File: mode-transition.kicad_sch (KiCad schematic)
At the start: 17 parts, among them Q19001 DNLS350E, U19001 4081, U19002 4073, U19003 4075, U19004 4081, U19005 4073, U19006 4075, U19007 4069

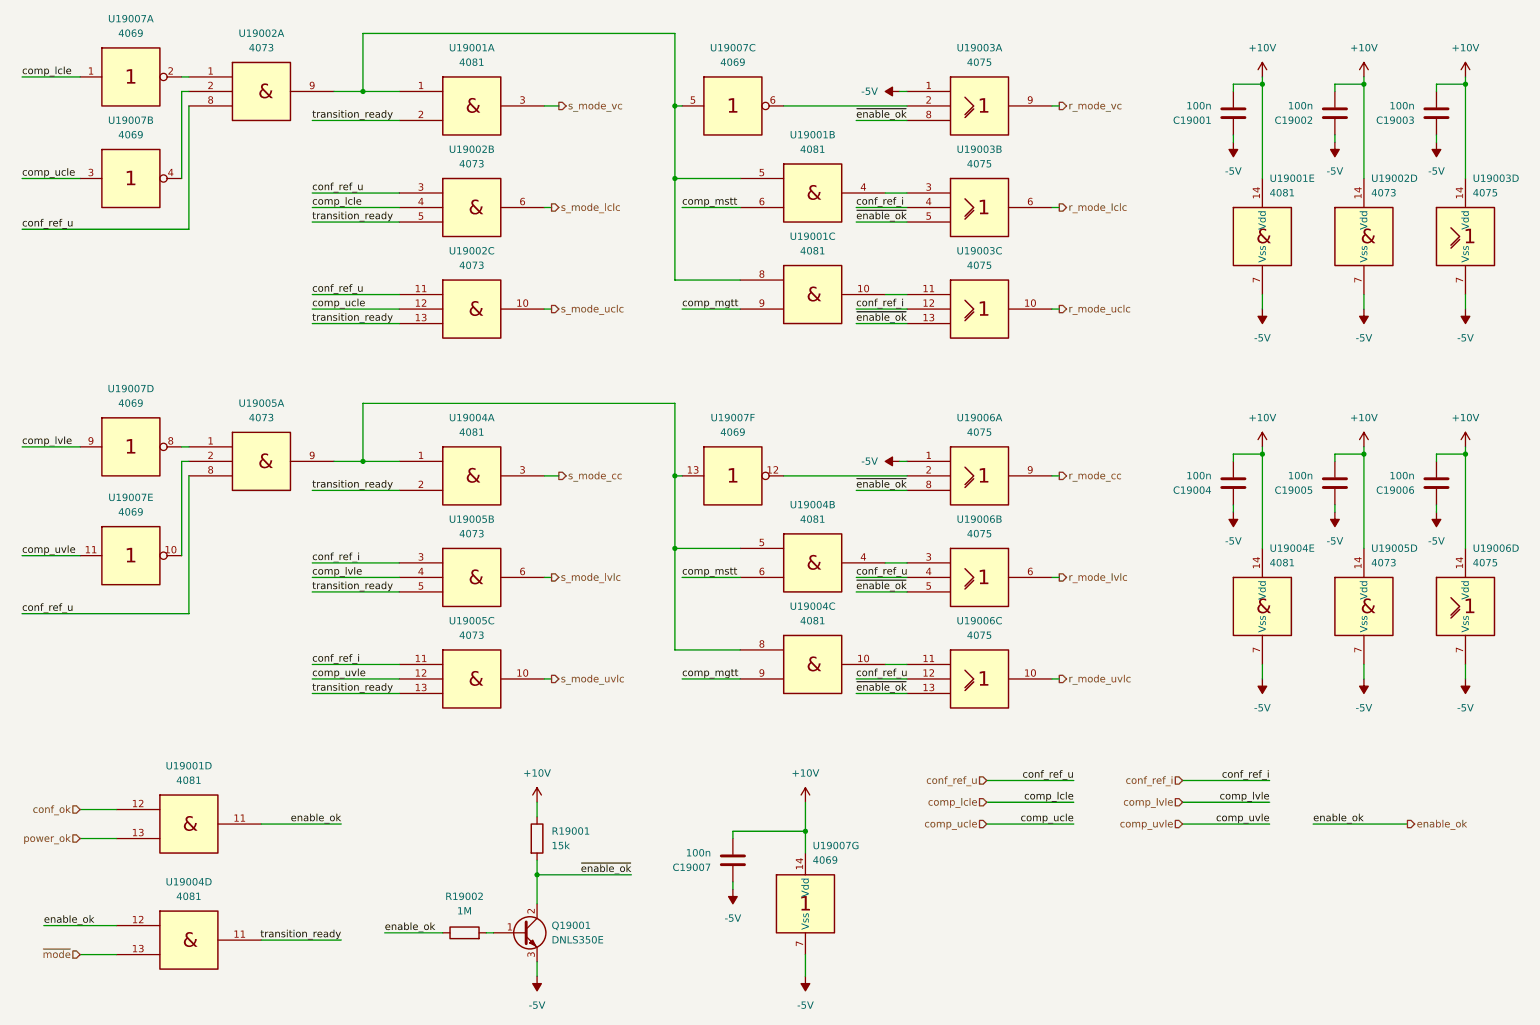
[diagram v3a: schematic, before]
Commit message: add limit-logic compare-logic hierachical sheet and hirarchy connectors
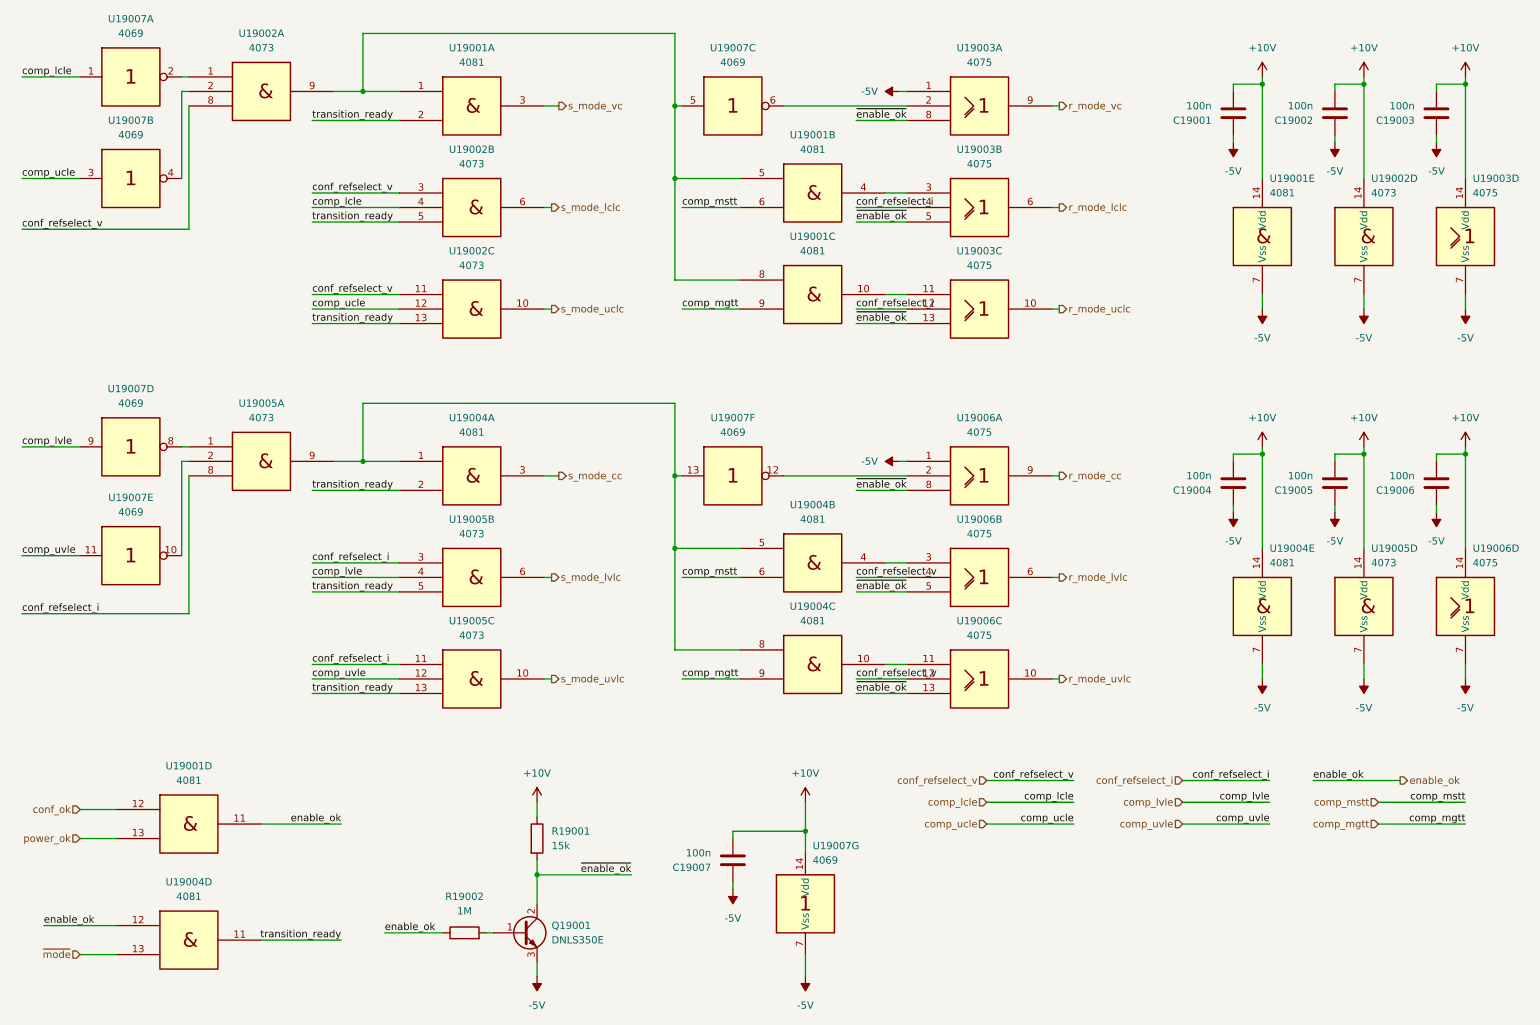
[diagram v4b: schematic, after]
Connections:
- net conf_ref_i renamed conf_refselect_i
- net conf_refselect_i: now also U19005.8
- net conf_ref_u renamed conf_refselect_v
- net conf_refselect_v: no longer U19005.8
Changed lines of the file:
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@@
+	(wire
+		(pts
+			(xy 257.81 160.02) (xy 273.05 160.02)
+		)
+		(stroke
+			(width 0)
+			(type default)
+		)
+	)
 	(wire
 		(pts
@@
 	(wire
 		(pts
+			(xy 49.53 99.06) (xy 49.53 123.19)
+		)
+		(stroke
+			(width 0)
+			(type default)
+		)
+	)
+	(wire
+		(pts
 			(xy 250.19 39.37) (xy 250.19 40.64)
 		)
@@
 	(wire
 		(pts
-			(xy 246.38 160.02) (xy 262.89 160.02)
+			(xy 246.38 152.4) (xy 261.62 152.4)
+		)
+		(stroke
+			(width 0)
+			(type default)
+		)
+	)
+	(wire
+		(pts
+			(xy 257.81 156.21) (xy 273.05 156.21)
 		)
 		(stroke
@@
 	(wire
 		(pts
-			(xy 49.53 123.19) (xy 49.53 99.06)
-		)
-		(stroke
-			(width 0)
-			(type default)
-		)
-	)
-	(wire
-		(pts
 			(xy 49.53 55.88) (xy 49.53 34.29)
 		)
@@
 			(width 0)
 			(type default)
+		)
+	)
+	(label "comp_mstt"
+		(at 273.05 156.21 180)
+		(fields_autoplaced yes)
+		(effects
+			(font
+				(size 1.27 1.27)
+			)
+			(justify right bottom)
 		)
 	)
@@
 		)
 	)
-	(label "conf_ref_i"
+	(label "conf_refselect_i"
 		(at 71.12 114.3 0)
 		(fields_autoplaced yes)
@@
 		)
 	)
-	(label "conf_ref_i"
+	(label "conf_refselect_i"
 		(at 166.37 52.07 0)
 		(fields_autoplaced yes)
@@
 		)
 	)
-	(label "conf_ref_u"
+	(label "conf_refselect_i"
 		(at 20.32 123.19 0)
 		(fields_autoplaced yes)
@@
 		)
 	)
-	(label "conf_ref_u"
+	(label "conf_refselect_v"
 		(at 204.47 152.4 180)
 		(fields_autoplaced yes)
@@
 		)
 	)
-	(label "conf_ref_i"
+	(label "conf_refselect_i"
 		(at 238.76 152.4 180)
 		(fields_autoplaced yes)
@@
 		)
 	)
-	(label "conf_ref_u"
+	(label "comp_mgtt"
+		(at 273.05 160.02 180)
+		(fields_autoplaced yes)
+		(effects
+			(font
+				(size 1.27 1.27)
+			)
+			(justify right bottom)
+		)
+	)
+	(label "conf_refselect_v"
 		(at 71.12 67.31 0)
 		(fields_autoplaced yes)
@@
 		)
 	)
-	(label "conf_ref_u"
+	(label "conf_refselect_v"
 		(at 166.37 134.62 0)
 		(fields_autoplaced yes)
@@
 		)
 	)
-	(label "conf_ref_i"
+	(label "conf_refselect_i"
 		(at 166.37 69.85 0)
 		(fields_autoplaced yes)
@@
 	)
 	(label "enable_ok"
-		(at 246.38 160.02 0)
+		(at 246.38 152.4 0)
 		(fields_autoplaced yes)
 		(effects
@@
 		)
 	)
-	(label "conf_ref_u"
+	(label "conf_refselect_v"
 		(at 71.12 49.53 0)
 		(fields_autoplaced yes)
@@
 		)
 	)
-	(label "conf_ref_i"
+	(label "conf_refselect_i"
 		(at 71.12 132.08 0)
 		(fields_autoplaced yes)
@@
 		)
 	)
-	(label "conf_ref_u"
+	(label "conf_refselect_v"
 		(at 166.37 116.84 0)
 		(fields_autoplaced yes)
@@
 		)
 	)
-	(label "conf_ref_u"
+	(label "conf_refselect_v"
 		(at 20.32 55.88 0)
 		(fields_autoplaced yes)
@@
 	(hierarchical_label "enable_ok"
 		(shape output)
-		(at 262.89 160.02 0)
+		(at 261.62 152.4 0)
 		(fields_autoplaced yes)
 		(effects
@@
 		)
 	)
+	(hierarchical_label "comp_mgtt"
+		(shape input)
+		(at 257.81 160.02 180)
+		(fields_autoplaced yes)
+		(effects
+			(font
+				(size 1.27 1.27)
+			)
+			(justify right)
+		)
+	)
 	(hierarchical_label "s_mode_uvlc"
 		(shape output)
@@
 		)
 	)
+	(hierarchical_label "comp_mstt"
+		(shape input)
+		(at 257.81 156.21 180)
+		(fields_autoplaced yes)
+		(effects
+			(font
+				(size 1.27 1.27)
+			)
+			(justify right)
+		)
+	)
 	(hierarchical_label "r_mode_lvlc"
 		(shape output)
@@
 		)
 	)
-	(hierarchical_label "conf_ref_u"
+	(hierarchical_label "conf_refselect_v"
 		(shape input)
 		(at 189.23 152.4 180)
@@
 		)
 	)
-	(hierarchical_label "conf_ref_i"
+	(hierarchical_label "conf_refselect_i"
 		(shape input)
 		(at 223.52 152.4 180)

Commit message: fix missing footprints, MPN, VPN and datasheet info in BOM
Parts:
- Q19001: footprint (none) -> Package_TO_SOT_SMD:SOT-223-3_TabPin2; MPN (none) -> DNLS350E-13; VPN (none) -> 621-DNLS350E-13
- U19003, U19006: footprint (none) -> Package_SO:SOIC-14_3.9x8.7mm_P1.27mm; MPN (none) -> CD4075BM96; VPN (none) -> 595-CD4075BM96
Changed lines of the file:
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@@
 			)
 		)
-		(property "Footprint" ""
+		(property "Footprint" "Package_SO:SOIC-14_3.9x8.7mm_P1.27mm"
 			(at 273.05 121.92 0)
 			(effects
@@
 			)
 		)
-		(property "Datasheet" ""
+		(property "Datasheet" "https://www.ti.com/lit/ds/symlink/cd4075b.pdf"
 			(at 273.05 121.92 0)
 			(effects
@@
 			)
 		)
+		(property "MPN" "CD4075BM96"
+			(at 273.05 121.92 0)
+			(effects
+				(font
+					(size 1.27 1.27)
+				)
+				(hide yes)
+			)
+		)
+		(property "VPN" "595-CD4075BM96"
+			(at 273.05 121.92 0)
+			(effects
+				(font
+					(size 1.27 1.27)
+				)
+				(hide yes)
+			)
+		)
 		(pin "1"
 		)
@@
 			)
 		)
-		(property "Footprint" ""
+		(property "Footprint" "Package_SO:SOIC-14_3.9x8.7mm_P1.27mm"
 			(at 187.96 99.06 0)
 			(effects
@@
 			)
 		)
-		(property "Datasheet" ""
+		(property "Datasheet" "https://www.ti.com/lit/ds/symlink/cd4075b.pdf"
 			(at 187.96 99.06 0)
 			(effects
@@
 			)
 		)
+		(property "MPN" "CD4075BM96"
+			(at 187.96 99.06 0)
+			(effects
+				(font
+					(size 1.27 1.27)
+				)
+				(hide yes)
+			)
+		)
+		(property "VPN" "595-CD4075BM96"
+			(at 187.96 99.06 0)
+			(effects
+				(font
+					(size 1.27 1.27)
+				)
+				(hide yes)
+			)
+		)
 		(pin "1"
 		)
@@
 			)
 		)
-		(property "Footprint" ""
+		(property "Footprint" "Package_SO:SOIC-14_3.9x8.7mm_P1.27mm"
 			(at 273.05 57.15 0)
 			(effects
@@
 			)
 		)
-		(property "Datasheet" ""
+		(property "Datasheet" "https://www.ti.com/lit/ds/symlink/cd4075b.pdf"
 			(at 273.05 57.15 0)
 			(effects
@@
 			)
 		)
+		(property "MPN" "CD4075BM96"
+			(at 273.05 57.15 0)
+			(effects
+				(font
+					(size 1.27 1.27)
+				)
+				(hide yes)
+			)
+		)
+		(property "VPN" "595-CD4075BM96"
+			(at 273.05 57.15 0)
+			(effects
+				(font
+					(size 1.27 1.27)
+				)
+				(hide yes)
+			)
+		)
 		(pin "1"
 		)
@@
 			)
 		)
-		(property "Footprint" ""
+		(property "Footprint" "Package_TO_SOT_SMD:SOT-223-3_TabPin2"
 			(at 113.03 176.53 0)
 			(effects
@@
 			)
 		)
-		(property "Datasheet" "~"
+		(property "Datasheet" "https://www.diodes.com/assets/Datasheets/ds31231.pdf"
 			(at 107.95 179.07 0)
 			(effects
@@
 			)
 		)
-		(property "MPN" ""
+		(property "MPN" "DNLS350E-13"
 			(at 107.95 179.07 0)
 			(effects
@@
 			)
 		)
-		(property "VPN" ""
+		(property "VPN" "621-DNLS350E-13"
 			(at 107.95 179.07 0)
 			(effects
@@
 			)
 		)
-		(property "Footprint" ""
+		(property "Footprint" "Package_SO:SOIC-14_3.9x8.7mm_P1.27mm"
 			(at 187.96 34.29 0)
 			(effects
@@
 			)
 		)
-		(property "Datasheet" ""
+		(property "Datasheet" "https://www.ti.com/lit/ds/symlink/cd4075b.pdf"
 			(at 187.96 34.29 0)
 			(effects
@@
 			)
 		)
+		(property "MPN" "CD4075BM96"
+			(at 187.96 34.29 0)
+			(effects
+				(font
+					(size 1.27 1.27)
+				)
+				(hide yes)
+			)
+		)
+		(property "VPN" "595-CD4075BM96"
+			(at 187.96 34.29 0)
+			(effects
+				(font
+					(size 1.27 1.27)
+				)
+				(hide yes)
+			)
+		)
 		(pin "1"
 		)
@@
 			)
 		)
-		(property "Footprint" ""
+		(property "Footprint" "Package_SO:SOIC-14_3.9x8.7mm_P1.27mm"
 			(at 187.96 116.84 0)
 			(effects
@@
 			)
 		)
-		(property "Datasheet" ""
+		(property "Datasheet" "https://www.ti.com/lit/ds/symlink/cd4075b.pdf"
 			(at 187.96 116.84 0)
 			(effects
@@
 			)
 		)
+		(property "MPN" "CD4075BM96"
+			(at 187.96 116.84 0)
+			(effects
+				(font
+					(size 1.27 1.27)
+				)
+				(hide yes)
+			)
+		)
+		(property "VPN" "595-CD4075BM96"
+			(at 187.96 116.84 0)
+			(effects
+				(font
+					(size 1.27 1.27)
+				)
+				(hide yes)
+			)
+		)
 		(pin "1"
 		)
@@
 			)
 		)
-		(property "Footprint" ""
+		(property "Footprint" "Package_SO:SOIC-14_3.9x8.7mm_P1.27mm"
 			(at 187.96 69.85 0)
 			(effects
@@
 			)
 		)
-		(property "Datasheet" ""
+		(property "Datasheet" "https://www.ti.com/lit/ds/symlink/cd4075b.pdf"
 			(at 187.96 69.85 0)
 			(effects
@@
 			)
 		)
+		(property "MPN" "CD4075BM96"
+			(at 187.96 69.85 0)
+			(effects
+				(font
+					(size 1.27 1.27)
+				)
+				(hide yes)
+			)
+		)
+		(property "VPN" "595-CD4075BM96"
+			(at 187.96 69.85 0)
+			(effects
+				(font
+					(size 1.27 1.27)
+				)
+				(hide yes)
+			)
+		)
 		(pin "1"
 		)
@@
 			)
 		)
-		(property "Footprint" ""
+		(property "Footprint" "Package_SO:SOIC-14_3.9x8.7mm_P1.27mm"
 			(at 187.96 52.07 0)
 			(effects
@@
 			)
 		)
-		(property "Datasheet" ""
+		(property "Datasheet" "https://www.ti.com/lit/ds/symlink/cd4075b.pdf"
 			(at 187.96 52.07 0)
 			(effects
@@
 			)
 		)
+		(property "MPN" "CD4075BM96"
+			(at 187.96 52.07 0)
+			(effects
+				(font
+					(size 1.27 1.27)
+				)
+				(hide yes)
+			)
+		)
+		(property "VPN" "595-CD4075BM96"
+			(at 187.96 52.07 0)
+			(effects
+				(font
+					(size 1.27 1.27)
+				)
+				(hide yes)
+			)
+		)
 		(pin "1"
 		)
@@
 			)
 		)
-		(property "Footprint" ""
+		(property "Footprint" "Package_SO:SOIC-14_3.9x8.7mm_P1.27mm"
 			(at 187.96 134.62 0)
 			(effects
@@
 			)
 		)
-		(property "Datasheet" ""
+		(property "Datasheet" "https://www.ti.com/lit/ds/symlink/cd4075b.pdf"
 			(at 187.96 134.62 0)
 			(effects
@@
 			(at 187.96 134.62 0)
 			(effects
+				(font
+					(size 1.27 1.27)
+				)
+				(hide yes)
+			)
+		)
+		(property "MPN" "CD4075BM96"
+			(at 187.96 134.62 0)
+			(effects
+				(font
+					(size 1.27 1.27)
+				)
+				(hide yes)
+			)
+		)
+		(property "VPN" "595-CD4075BM96"
+			(at 187.96 134.62 0)
+			(effects

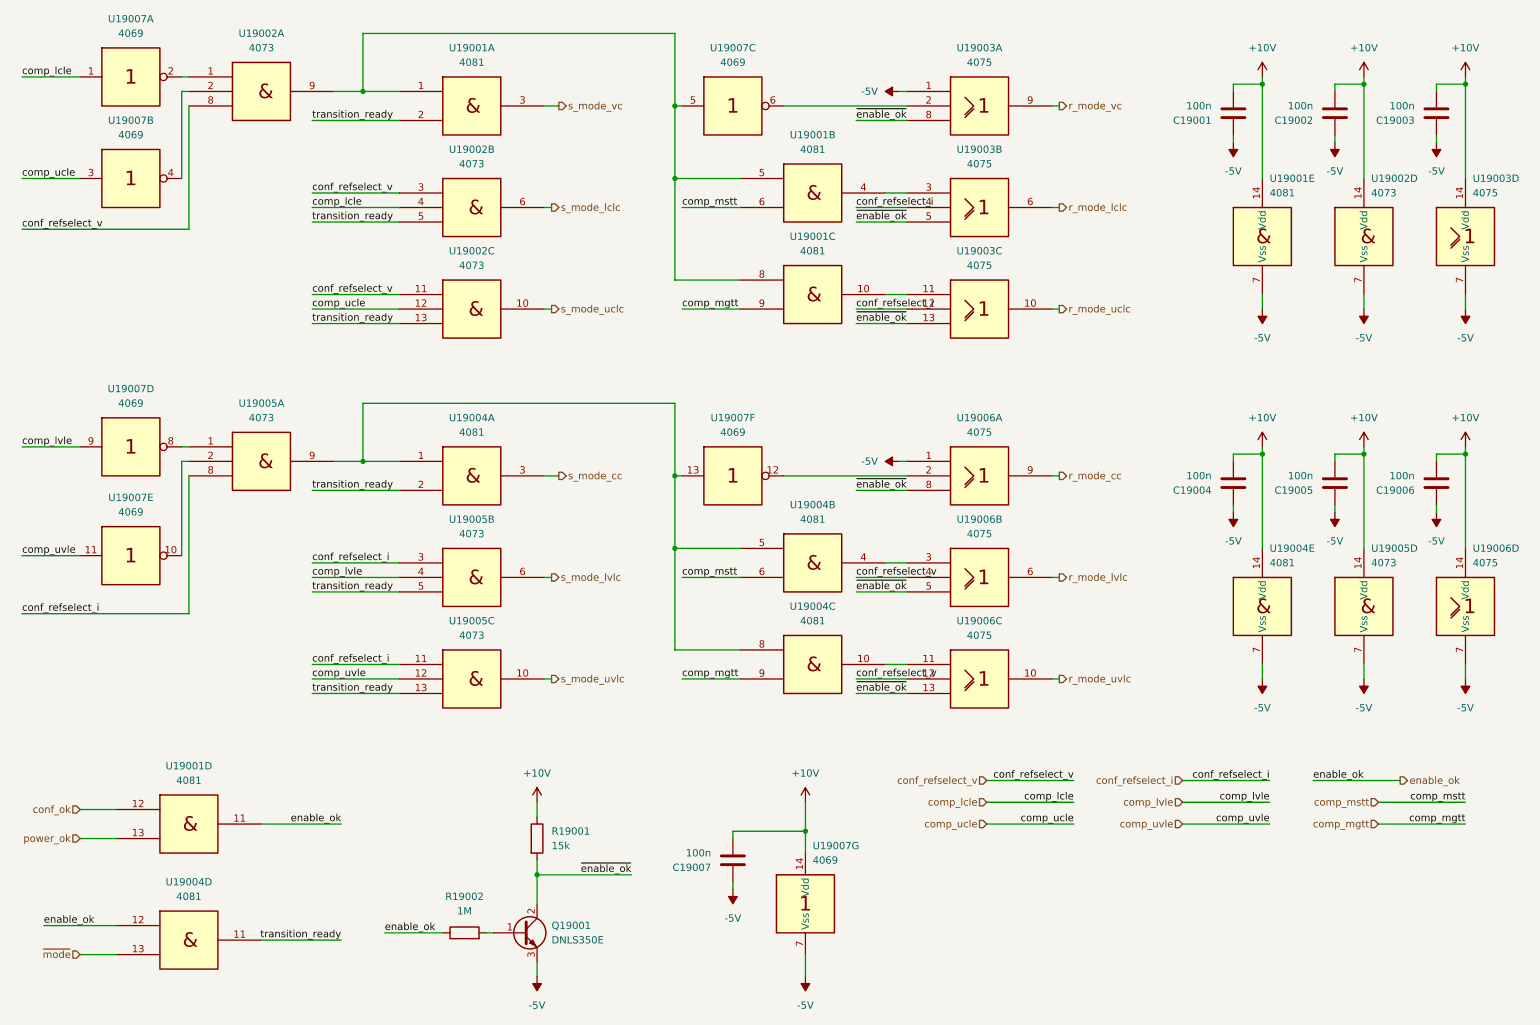
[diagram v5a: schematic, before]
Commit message: remove control-logic hierarchical parent sheet
Sheet is unnecessary for system overview and hides details of the structure, that should be presented.
Removing the sheet also allows to make a clear separation of the power electronics, controller and measurement for
multi PCB Layout. This separation would be hidden away with the control-logic super sheet and would cut through
multiple hierarchical layers.
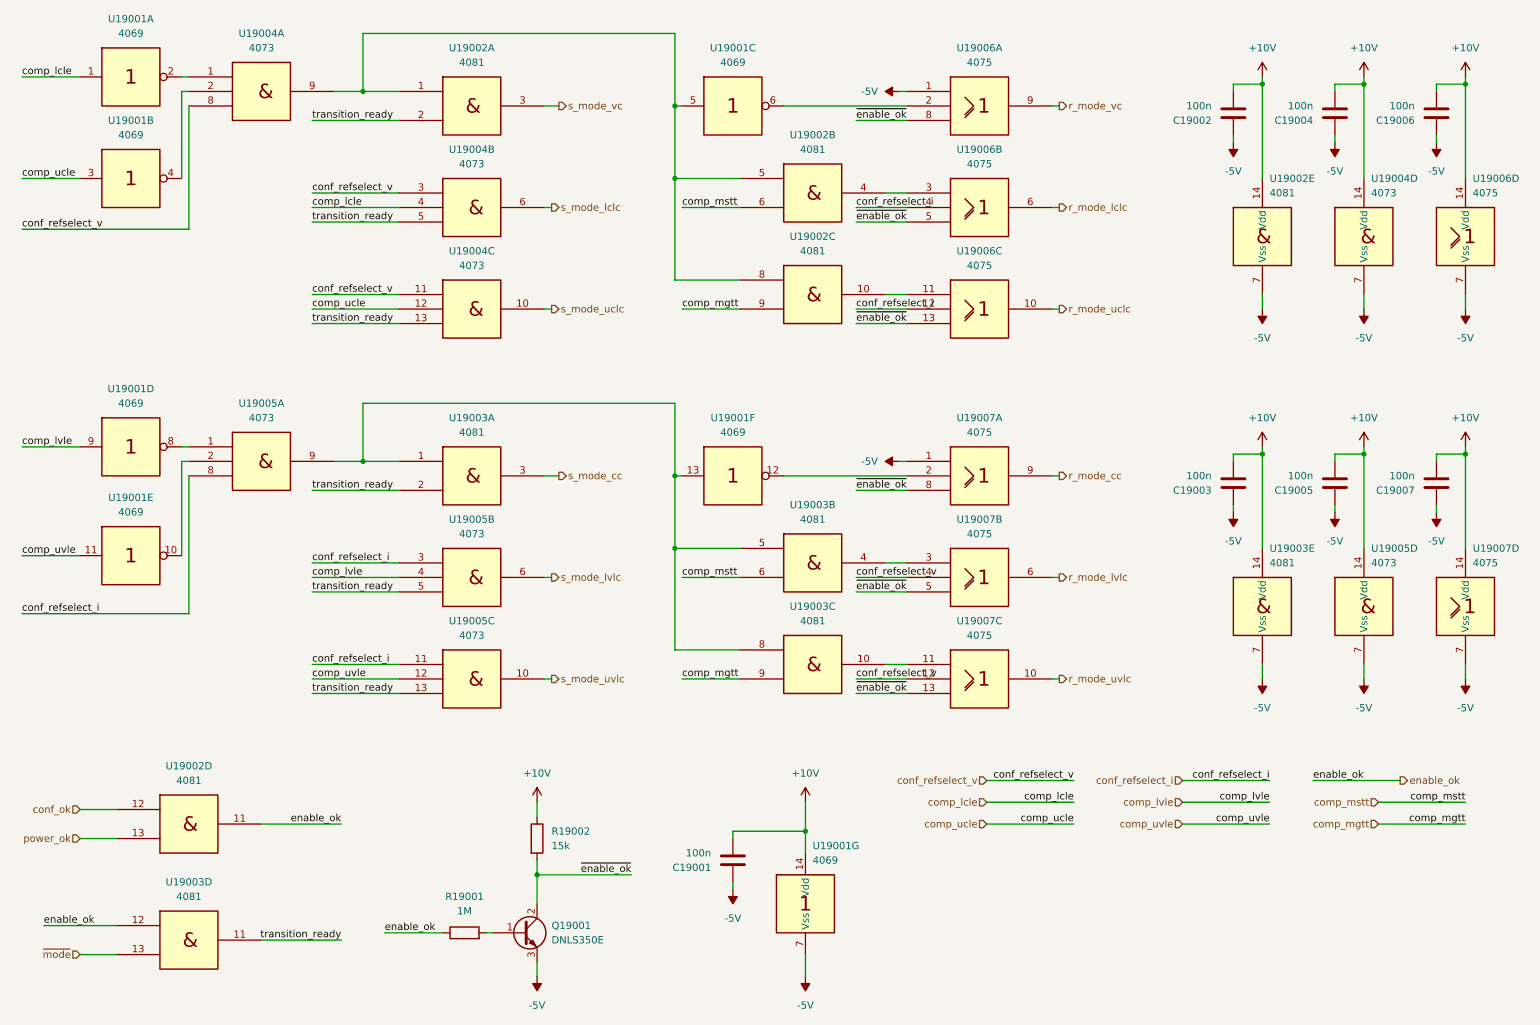
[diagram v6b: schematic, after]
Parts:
- renumbered C19007 to C19001, C19001 to C19002, C19004 to C19003, C19002 to C19004, C19003 to C19006, C19006 to C19007, R19002 to R19001, R19001 to R19002, U19007 to U19001, U19001 to U19002, U19004 to U19003, U19002 to U19004, U19003 to U19006, U19006 to U19007
